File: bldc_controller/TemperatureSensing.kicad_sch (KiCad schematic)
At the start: 7 parts

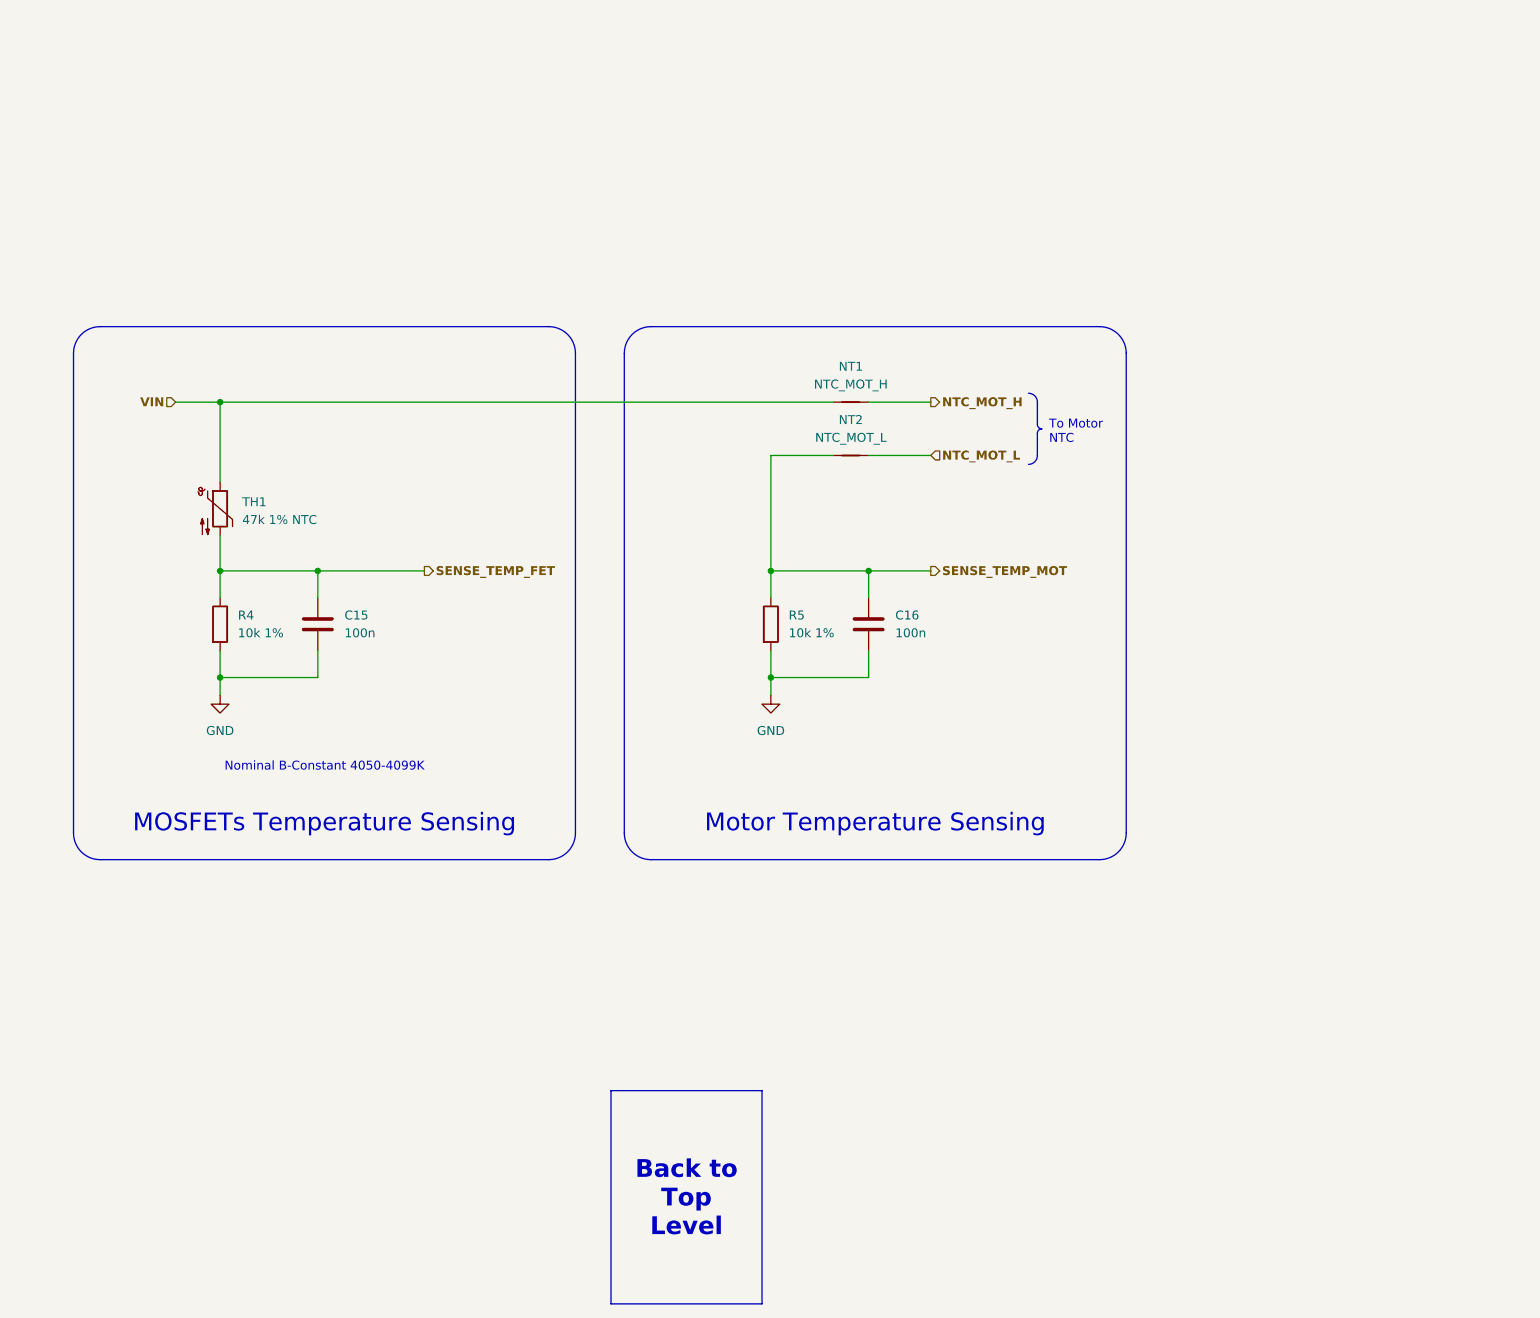
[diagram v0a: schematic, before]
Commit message: added temporary footprints and deleted extra files
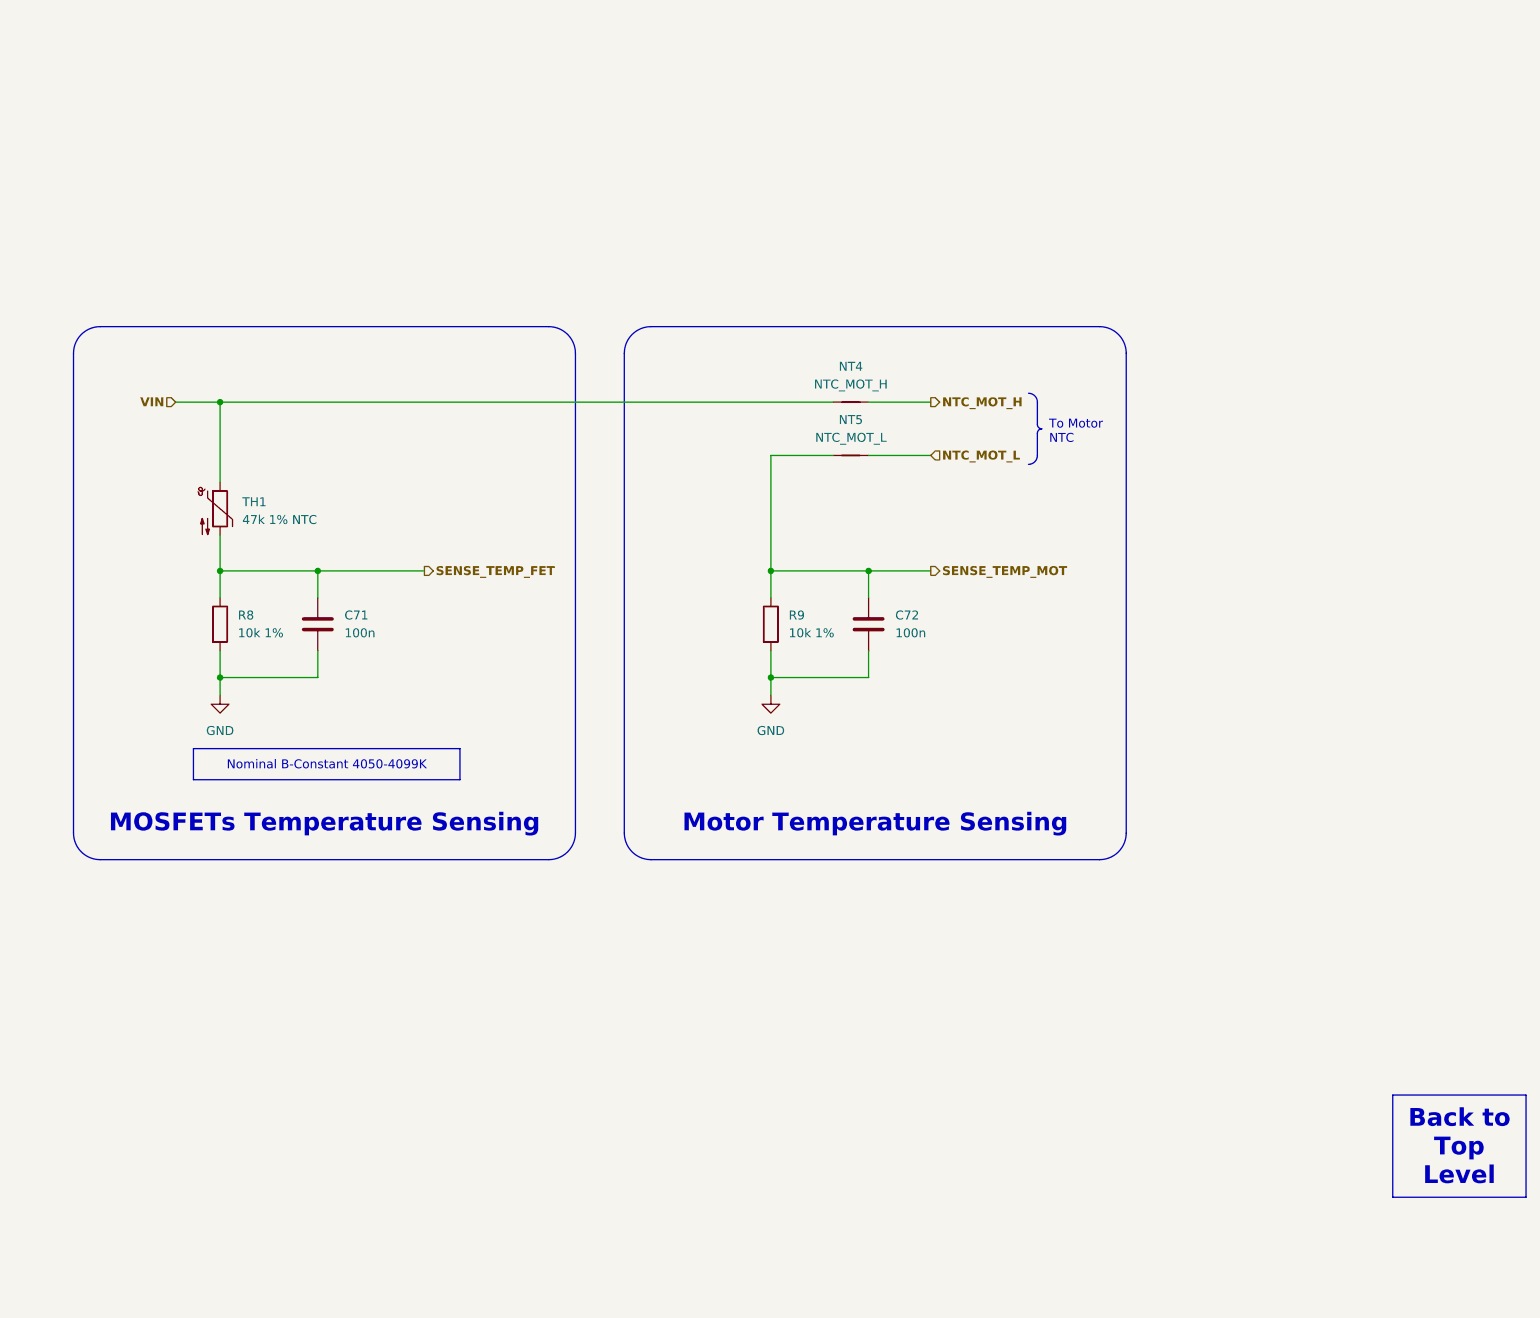
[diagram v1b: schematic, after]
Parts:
- C71: renamed from C15; footprint (none) -> Capacitor_SMD:C_0402_1005Metric
- C72: renamed from C16; footprint (none) -> Capacitor_SMD:C_0402_1005Metric
- NT4: renamed from NT1; footprint (none) -> NetTie:NetTie-2_SMD_Pad0.5mm
- NT5: renamed from NT2; footprint (none) -> NetTie:NetTie-2_SMD_Pad0.5mm
- R8: renamed from R4; footprint (none) -> Resistor_SMD:R_0402_1005Metric
- R9: renamed from R5; footprint (none) -> Resistor_SMD:R_0402_1005Metric
- TH1: footprint (none) -> Resistor_SMD:R_0402_1005Metric
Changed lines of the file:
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@@
     (fill (type none))
+  )
+  (text_box "Back to Top Level"
+    (at 265.43 166.37 0) (size 19.05 14.605)
+    (stroke (width 0) (type default) (color 0 0 0 1))
+    (fill (type color) (color 0 0 0 0.1))
+    (effects (font (size 2.54 2.54) (thickness 0.508) bold (color 0 0 0 1)) (href "#1"))
   )
   (text_box "To Motor NTC"
@@
     (effects (font (size 1.27 1.27)) (justify left top))
   )
-  (text_box "Back to Top Level"
-    (at 153.67 165.735 0) (size 21.59 30.48)
-    (stroke (width 0) (type default) (color 0 0 0 1))
-    (fill (type color) (color 0 0 0 0.1))
-    (effects (font (size 2.54 2.54) (thickness 0.508) bold (color 0 0 0 1)) (href "#1"))
-  )
   (text_box "Motor Temperature Sensing"
     (at 158.115 121.285 0) (size 66.675 9.525)
     (stroke (width -0.0001) (type default))
     (fill (type none))
-    (effects (font (size 2.54 2.54) (color 0 0 0 1)) (justify bottom))
+    (effects (font (size 2.54 2.54) (thickness 0.508) bold (color 0 0 0 1)) (justify bottom))
   )
   (text_box "MOSFETs Temperature Sensing"
@@
     (stroke (width -0.0001) (type default))
     (fill (type none))
-    (effects (font (size 2.54 2.54) (color 0 0 0 1)) (justify bottom))
+    (effects (font (size 2.54 2.54) (thickness 0.508) bold (color 0 0 0 1)) (justify bottom))
   )
   (text_box "Nominal B-Constant 4050-4099K"
-    (at 90.17 117.475 0) (size 45.085 8.255)
-    (stroke (width -0.0001) (type default))
-    (fill (type none))
-    (effects (font (size 1.27 1.27)) (justify top))
+    (at 93.98 116.84 0) (size 38.1 4.445)
+    (stroke (width 0) (type default) (color 0 0 0 1))
+    (fill (type color) (color 191 240 255 1))
+    (effects (font (size 1.27 1.27) (color 0 0 0 1)))
   )
   (hierarchical_label "VIN" (shape input) (at 91.44 67.31 180) (fields_autoplaced)
@@
   (symbol (lib_id "Device:NetTie_2") (at 187.96 67.31 0) (unit 1)
     (in_bom no) (on_board yes) (dnp no) (fields_autoplaced)
-    (property "Reference" "NT1" (at 187.96 62.23 0)
+    (property "Reference" "NT4" (at 187.96 62.23 0)
       (effects (font (size 1.27 1.27)))
     )
@@
       (effects (font (size 1.27 1.27)))
     )
-    (property "Footprint" "" (at 187.96 67.31 0)
+    (property "Footprint" "NetTie:NetTie-2_SMD_Pad0.5mm" (at 187.96 67.31 0)
       (effects (font (size 1.27 1.27)) hide)
     )
@@
       (project "bldc_controller"
         (path "/0650c7a8-acba-429c-9f8e-eec0baf0bc1c/ce1ea51b-4118-4fb5-9a41-40670da86eb7"
-          (reference "NT1") (unit 1)
+          (reference "NT4") (unit 1)
         )
       )
@@
   (symbol (lib_id "power:GND") (at 176.53 109.22 0) (unit 1)
     (in_bom yes) (on_board yes) (dnp no) (fields_autoplaced)
-    (property "Reference" "#PWR019" (at 176.53 115.57 0)
+    (property "Reference" "#PWR023" (at 176.53 115.57 0)
       (effects (font (size 1.27 1.27)) hide)
     )
@@
       (project "bldc_controller"
         (path "/0650c7a8-acba-429c-9f8e-eec0baf0bc1c/ce1ea51b-4118-4fb5-9a41-40670da86eb7"
-          (reference "#PWR019") (unit 1)
+          (reference "#PWR023") (unit 1)
         )
       )
@@
   (symbol (lib_id "Device:R") (at 97.79 99.06 0) (unit 1)
     (in_bom yes) (on_board yes) (dnp no) (fields_autoplaced)
-    (property "Reference" "R4" (at 100.33 97.79 0)
+    (property "Reference" "R8" (at 100.33 97.79 0)
       (effects (font (size 1.27 1.27)) (justify left))
     )
@@
       (effects (font (size 1.27 1.27)) (justify left))
     )
-    (property "Footprint" "" (at 96.012 99.06 90)
+    (property "Footprint" "Resistor_SMD:R_0402_1005Metric" (at 96.012 99.06 90)
       (effects (font (size 1.27 1.27)) hide)
     )
@@
       (project "bldc_controller"
         (path "/0650c7a8-acba-429c-9f8e-eec0baf0bc1c/ce1ea51b-4118-4fb5-9a41-40670da86eb7"
-          (reference "R4") (unit 1)
+          (reference "R8") (unit 1)
         )
       )
@@
   (symbol (lib_id "Device:R") (at 176.53 99.06 0) (unit 1)
     (in_bom yes) (on_board yes) (dnp no) (fields_autoplaced)
-    (property "Reference" "R5" (at 179.07 97.79 0)
+    (property "Reference" "R9" (at 179.07 97.79 0)
       (effects (font (size 1.27 1.27)) (justify left))
     )
@@
       (effects (font (size 1.27 1.27)) (justify left))
     )
-    (property "Footprint" "" (at 174.752 99.06 90)
+    (property "Footprint" "Resistor_SMD:R_0402_1005Metric" (at 174.752 99.06 90)
       (effects (font (size 1.27 1.27)) hide)
     )
@@
       (project "bldc_controller"
         (path "/0650c7a8-acba-429c-9f8e-eec0baf0bc1c/ce1ea51b-4118-4fb5-9a41-40670da86eb7"
-          (reference "R5") (unit 1)
+          (reference "R9") (unit 1)
         )
       )
@@
   (symbol (lib_id "Device:C") (at 111.76 99.06 0) (unit 1)
     (in_bom yes) (on_board yes) (dnp no) (fields_autoplaced)
-    (property "Reference" "C15" (at 115.57 97.79 0)
+    (property "Reference" "C71" (at 115.57 97.79 0)
       (effects (font (size 1.27 1.27)) (justify left))
     )
@@
       (effects (font (size 1.27 1.27)) (justify left))
     )
-    (property "Footprint" "" (at 112.7252 102.87 0)
+    (property "Footprint" "Capacitor_SMD:C_0402_1005Metric" (at 112.7252 102.87 0)
       (effects (font (size 1.27 1.27)) hide)
     )
@@
       (project "bldc_controller"
         (path "/0650c7a8-acba-429c-9f8e-eec0baf0bc1c/ce1ea51b-4118-4fb5-9a41-40670da86eb7"
-          (reference "C15") (unit 1)
+          (reference "C71") (unit 1)
         )
       )
@@
   (symbol (lib_id "power:GND") (at 97.79 109.22 0) (unit 1)
     (in_bom yes) (on_board yes) (dnp no) (fields_autoplaced)
-    (property "Reference" "#PWR015" (at 97.79 115.57 0)
+    (property "Reference" "#PWR022" (at 97.79 115.57 0)
       (effects (font (size 1.27 1.27)) hide)
     )
@@
       (project "bldc_controller"
         (path "/0650c7a8-acba-429c-9f8e-eec0baf0bc1c/ce1ea51b-4118-4fb5-9a41-40670da86eb7"
-          (reference "#PWR015") (unit 1)
+          (reference "#PWR022") (unit 1)
         )
       )
@@
       (effects (font (size 1.27 1.27)) (justify left))
     )
-    (property "Footprint" "" (at 97.79 81.28 0)
+    (property "Footprint" "Resistor_SMD:R_0402_1005Metric" (at 97.79 81.28 0)
       (effects (font (size 1.27 1.27)) hide)
     )
@@
   (symbol (lib_id "Device:NetTie_2") (at 187.96 74.93 0) (unit 1)
     (in_bom no) (on_board yes) (dnp no)
-    (property "Reference" "NT2" (at 187.96 69.85 0)
+    (property "Reference" "NT5" (at 187.96 69.85 0)
       (effects (font (size 1.27 1.27)))
     )
@@
       (effects (font (size 1.27 1.27)))
     )
-    (property "Footprint" "" (at 187.96 74.93 0)
+    (property "Footprint" "NetTie:NetTie-2_SMD_Pad0.5mm" (at 187.96 74.93 0)
       (effects (font (size 1.27 1.27)) hide)
     )
@@
       (project "bldc_controller"
         (path "/0650c7a8-acba-429c-9f8e-eec0baf0bc1c/ce1ea51b-4118-4fb5-9a41-40670da86eb7"
-          (reference "NT2") (unit 1)
+          (reference "NT5") (unit 1)
         )
       )
@@
   (symbol (lib_id "Device:C") (at 190.5 99.06 0) (unit 1)
     (in_bom yes) (on_board yes) (dnp no) (fields_autoplaced)
-    (property "Reference" "C16" (at 194.31 97.79 0)
+    (property "Reference" "C72" (at 194.31 97.79 0)
       (effects (font (size 1.27 1.27)) (justify left))
     )
@@
       (effects (font (size 1.27 1.27)) (justify left))
     )
-    (property "Footprint" "" (at 191.4652 102.87 0)
+    (property "Footprint" "Capacitor_SMD:C_0402_1005Metric" (at 191.4652 102.87 0)
       (effects (font (size 1.27 1.27)) hide)
     )
@@
       (project "bldc_controller"
         (path "/0650c7a8-acba-429c-9f8e-eec0baf0bc1c/ce1ea51b-4118-4fb5-9a41-40670da86eb7"
-          (reference "C16") (unit 1)
-        )
-      )
+          (reference "C72") (unit 1)
+        )
+      )

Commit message: added IPC-7351 compliant footprints and started routing
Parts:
- C71, C72: footprint Capacitor_SMD:C_0402_1005Metric -> 0_capacitor_smd:C_0402_1005_DensityHigh
- NT4, NT5: footprint NetTie:NetTie-2_SMD_Pad0.5mm -> 0_net_tie:NetTie-2_SMD_Pad0.2mm
- R8, R9, TH1: footprint Resistor_SMD:R_0402_1005Metric -> 0_resistor_smd:R_0402_1005_DensityHigh
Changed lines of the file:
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@@
       (effects (font (size 1.27 1.27)))
     )
-    (property "Footprint" "NetTie:NetTie-2_SMD_Pad0.5mm" (at 187.96 67.31 0)
+    (property "Footprint" "0_net_tie:NetTie-2_SMD_Pad0.2mm" (at 187.96 67.31 0)
       (effects (font (size 1.27 1.27)) hide)
     )
@@
       (effects (font (size 1.27 1.27)) (justify left))
     )
-    (property "Footprint" "Resistor_SMD:R_0402_1005Metric" (at 96.012 99.06 90)
+    (property "Footprint" "0_resistor_smd:R_0402_1005_DensityHigh" (at 96.012 99.06 90)
       (effects (font (size 1.27 1.27)) hide)
     )
@@
       (effects (font (size 1.27 1.27)) (justify left))
     )
-    (property "Footprint" "Resistor_SMD:R_0402_1005Metric" (at 174.752 99.06 90)
+    (property "Footprint" "0_resistor_smd:R_0402_1005_DensityHigh" (at 174.752 99.06 90)
       (effects (font (size 1.27 1.27)) hide)
     )
@@
       (effects (font (size 1.27 1.27)) (justify left))
     )
-    (property "Footprint" "Capacitor_SMD:C_0402_1005Metric" (at 112.7252 102.87 0)
+    (property "Footprint" "0_capacitor_smd:C_0402_1005_DensityHigh" (at 112.7252 102.87 0)
       (effects (font (size 1.27 1.27)) hide)
     )
@@
       (effects (font (size 1.27 1.27)) (justify left))
     )
-    (property "Footprint" "Resistor_SMD:R_0402_1005Metric" (at 97.79 81.28 0)
+    (property "Footprint" "0_resistor_smd:R_0402_1005_DensityHigh" (at 97.79 81.28 0)
       (effects (font (size 1.27 1.27)) hide)
     )
@@
       (effects (font (size 1.27 1.27)))
     )
-    (property "Footprint" "NetTie:NetTie-2_SMD_Pad0.5mm" (at 187.96 74.93 0)
+    (property "Footprint" "0_net_tie:NetTie-2_SMD_Pad0.2mm" (at 187.96 74.93 0)
       (effects (font (size 1.27 1.27)) hide)
     )
@@
       (effects (font (size 1.27 1.27)) (justify left))
     )
-    (property "Footprint" "Capacitor_SMD:C_0402_1005Metric" (at 191.4652 102.87 0)
+    (property "Footprint" "0_capacitor_smd:C_0402_1005_DensityHigh" (at 191.4652 102.87 0)
       (effects (font (size 1.27 1.27)) hide)
     )
